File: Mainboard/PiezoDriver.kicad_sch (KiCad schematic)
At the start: 30 parts, among them U3 TL072, U4 TL072

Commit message: working mainboard push!
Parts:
- C10, C11, C12, C13, C14, C15: footprint (none) -> Capacitor_SMD:C_0805_2012Metric; Mouser Part Number (none) -> 80-C0805C472J3GAUTO
- C17, C18: footprint Capacitor_SMD:C_0603_1608Metric_Pad1.05x0.95mm_HandSolder -> Capacitor_SMD:C_0805_2012Metric; Mouser Part Number (none) -> 80-C0805S104K1RACAUT
- C19, C20: value 10u -> 100n; footprint Capacitor_SMD:C_0805_2012Metric_Pad1.15x1.40mm_HandSolder -> Capacitor_SMD:C_0805_2012Metric; LCSC C15850 -> C14663; Mouser Part Number (none) -> 80-C0805S104K1RACAUT
- R20, R22, R23, R25, R26, R27, R28, R29, R31, R32, R33, R34, R35, R36: footprint (none) -> Resistor_SMD:R_0805_2012Metric; Mouser Part Number (none) -> 667-ERA-6AED302V
- R21, R24, R37, R38: footprint (none) -> Resistor_SMD:R_0805_2012Metric; Mouser Part Number (none) -> 279-CRGH0805F220R
- U3, U4: footprint (none) -> Package_SO:SOIC-8-1EP_3.9x4.9mm_P1.27mm_EP2.29x3mm_ThermalVias; Mouser Part Number (none) -> 511-TL072BIDT
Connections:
- net +15V: now also C20.1, U3.8 (V+), U4.8 (V+); no longer C19.1
- net -15V: now also C19.2; no longer C20.2
- net GND: now also C19.1, C20.2; no longer C19.2, C20.1
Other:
- moved on the sheet: C13, R34

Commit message: cad update
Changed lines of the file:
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@@
 					(size 1.27 1.27)
 				)
+				(hide yes)
 			)
 		)
@@
 					(size 1.27 1.27)
 				)
-			)
-		)
+				(hide yes)
+			)
+		)

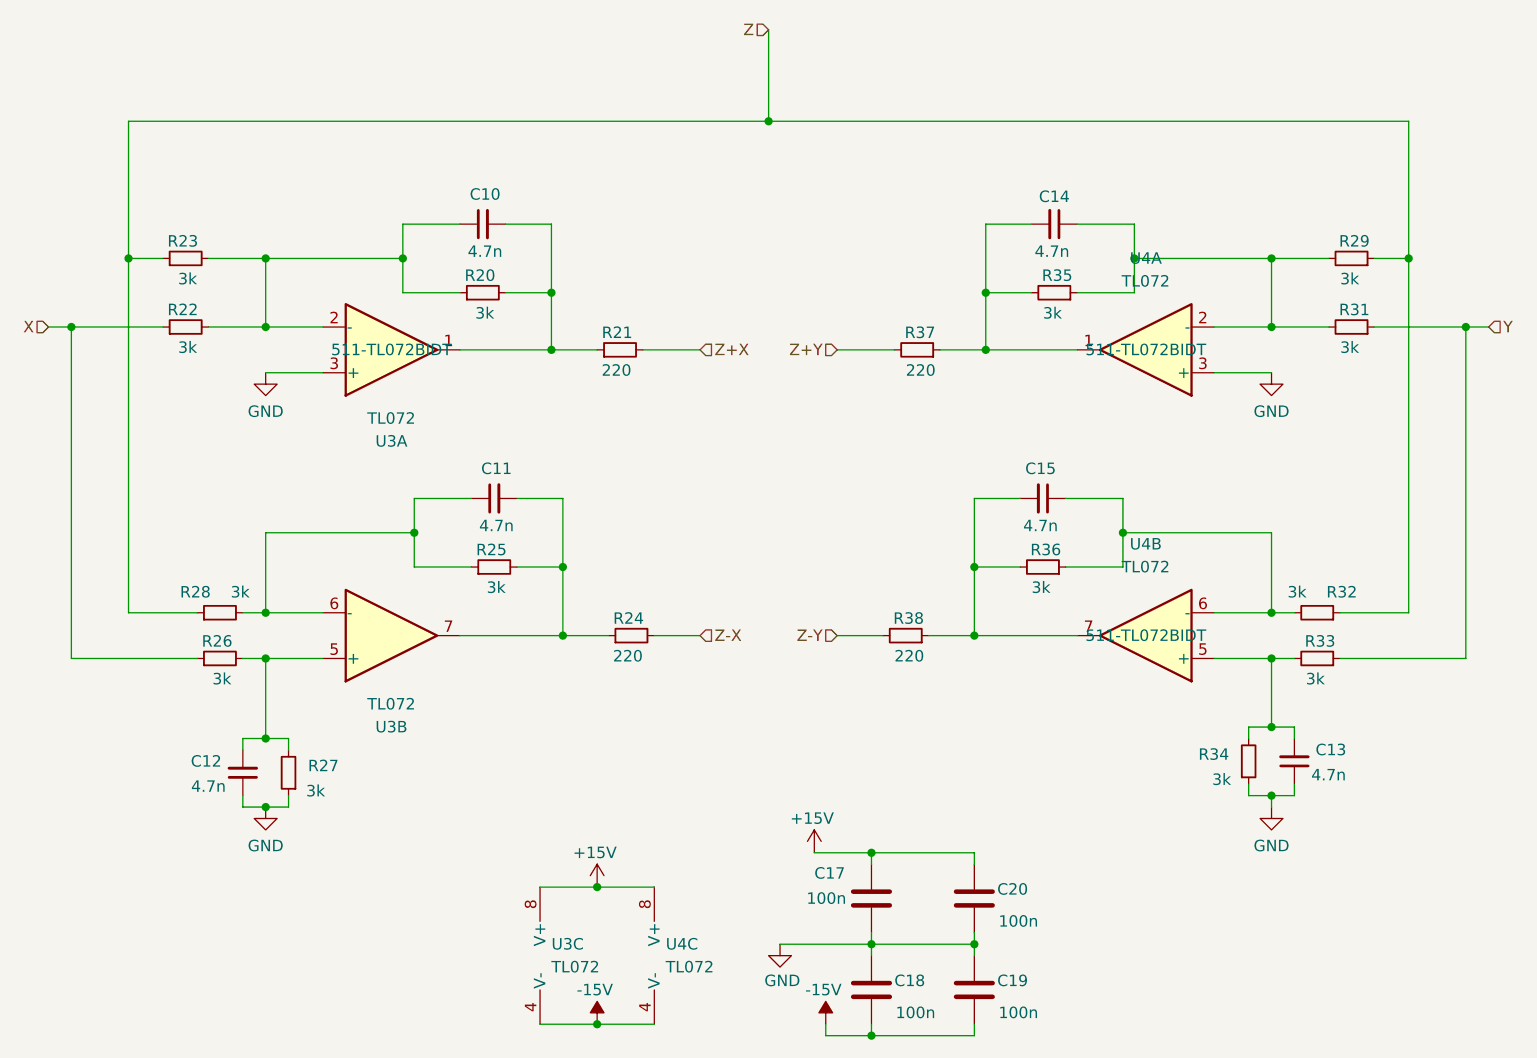
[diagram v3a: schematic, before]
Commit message: updates to DAC + ADC Libraries
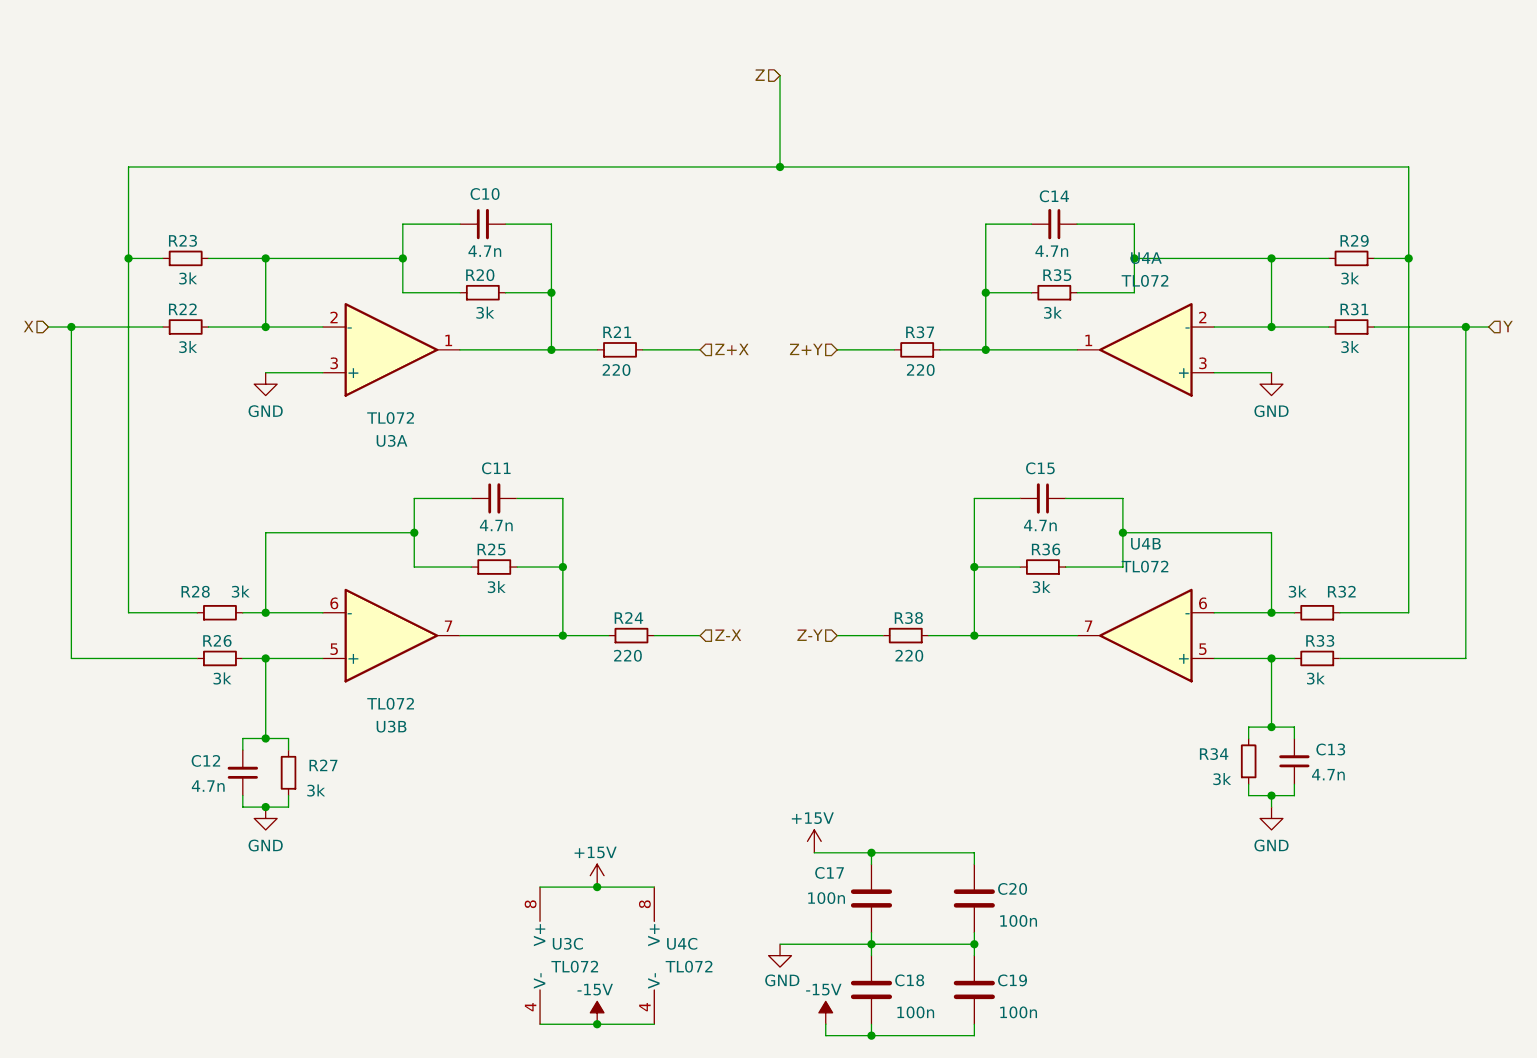
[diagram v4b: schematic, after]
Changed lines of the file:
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@@
 	)
 	(junction
-		(at 125.73 30.48)
-		(diameter 0)
-		(color 0 0 0 0)
-	)
-	(junction
 		(at 69.85 53.34)
 		(diameter 0)
@@
 	)
 	(junction
+		(at 127 35.56)
+		(diameter 0)
+		(color 0 0 0 0)
+	)
+	(junction
 		(at 181.61 45.72)
 		(diameter 0)
@@
 	(wire
 		(pts
-			(xy 54.61 30.48) (xy 125.73 30.48)
+			(xy 54.61 35.56) (xy 127 35.56)
 		)
 		(stroke
@@
 	(wire
 		(pts
-			(xy 196.85 30.48) (xy 196.85 45.72)
+			(xy 196.85 35.56) (xy 196.85 45.72)
 		)
 		(stroke
@@
 	(wire
 		(pts
-			(xy 125.73 30.48) (xy 196.85 30.48)
-		)
-		(stroke
-			(width 0)
-			(type default)
-		)
-	)
-	(wire
-		(pts
 			(xy 184.15 105.41) (xy 184.15 104.14)
 		)
@@
 	(wire
 		(pts
+			(xy 127 35.56) (xy 196.85 35.56)
+		)
+		(stroke
+			(width 0)
+			(type default)
+		)
+	)
+	(wire
+		(pts
 			(xy 181.61 105.41) (xy 179.07 105.41)
 		)
@@
 	(wire
 		(pts
-			(xy 54.61 30.48) (xy 54.61 45.72)
+			(xy 54.61 35.56) (xy 54.61 45.72)
 		)
 		(stroke
@@
 	(wire
 		(pts
-			(xy 125.73 30.48) (xy 125.73 20.32)
+			(xy 127 35.56) (xy 127 25.4)
 		)
 		(stroke
@@
 	(hierarchical_label "Z"
 		(shape input)
-		(at 125.73 20.32 180)
+		(at 127 25.4 180)
 		(effects
 			(font
@@
 					(size 1.27 1.27)
 				)
+				(hide yes)
 			)
 		)
@@
 					(size 1.27 1.27)
 				)
+				(hide yes)
 			)
 		)
@@
 					(size 1.27 1.27)
 				)
+				(hide yes)
 			)
 		)
